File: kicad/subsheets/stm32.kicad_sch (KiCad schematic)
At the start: 11 parts, among them U3 STM32U575RGT6

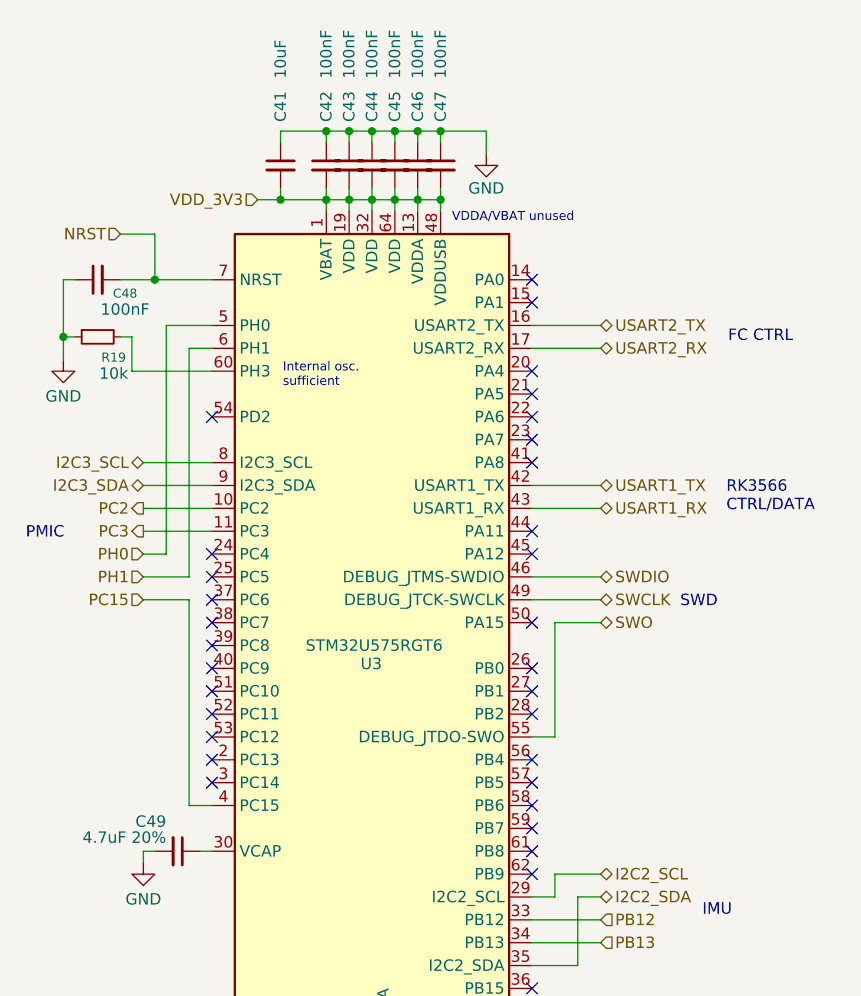
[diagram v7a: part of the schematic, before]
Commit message: Added boot + power switch to STM32, user button
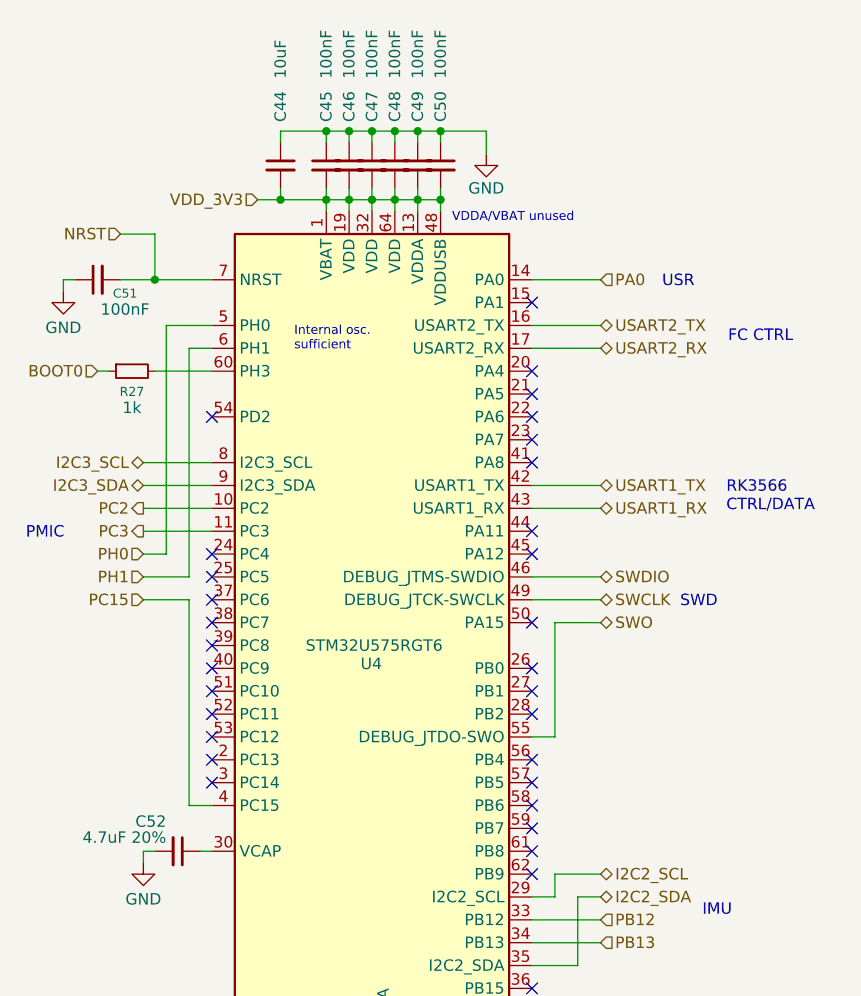
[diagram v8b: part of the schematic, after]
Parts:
- R27: renamed from R19; value 10k -> 1k
- renumbered C41 to C44, C42 to C45, C43 to C46, C44 to C47, C45 to C48, C46 to C49, C47 to C50, C48 to C51, C49 to C52, U3 to U4
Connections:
- net GND: no longer R27.1
- net PA0: now reaches U4.14 (PA0)
- new net BOOT0: R27.1
- no-connect marks 32 -> 31
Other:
- note added: "USR"
- moved on the sheet: R27
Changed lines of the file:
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@@
 		)
 	)
+	(text "USR"
+		(exclude_from_sim no)
+		(at 103.886 45.974 0)
+		(effects
+			(font
+				(size 1.27 1.27)
+			)
+		)
+	)
 	(text "RK3566 \nCTRL/DATA"
 		(exclude_from_sim no)
@@
 	(text "Internal osc.\nsufficient"
 		(exclude_from_sim no)
-		(at 59.944 56.388 0)
+		(at 61.214 52.324 0)
 		(effects
 			(font
@@
 	)
 	(junction
-		(at 35.56 52.07)
-		(diameter 0)
-		(color 0 0 0 0)
-	)
-	(junction
 		(at 45.72 45.72)
 		(diameter 0)
@@
 	)
 	(no_connect
-		(at 87.63 45.72)
-	)
-	(no_connect
 		(at 52.07 88.9)
 	)
@@
 	(wire
 		(pts
-			(xy 43.18 55.88) (xy 52.07 55.88)
-		)
-		(stroke
-			(width 0)
-			(type default)
-		)
-	)
-	(wire
-		(pts
 			(xy 44.45 76.2) (xy 46.99 76.2)
 		)
@@
 	(wire
 		(pts
-			(xy 35.56 54.61) (xy 35.56 52.07)
+			(xy 35.56 45.72) (xy 35.56 46.99)
 		)
 		(stroke
@@
 	(wire
 		(pts
-			(xy 41.91 52.07) (xy 43.18 52.07)
-		)
-		(stroke
-			(width 0)
-			(type default)
-		)
-	)
-	(wire
-		(pts
 			(xy 64.77 36.83) (xy 67.31 36.83)
 		)
@@
 	(wire
 		(pts
+			(xy 45.72 55.88) (xy 52.07 55.88)
+		)
+		(stroke
+			(width 0)
+			(type default)
+		)
+	)
+	(wire
+		(pts
 			(xy 74.93 35.56) (xy 74.93 36.83)
 		)
@@
 	(wire
 		(pts
-			(xy 35.56 52.07) (xy 36.83 52.07)
+			(xy 39.37 55.88) (xy 40.64 55.88)
 		)
 		(stroke
@@
 	(wire
 		(pts
-			(xy 43.18 52.07) (xy 43.18 55.88)
-		)
-		(stroke
-			(width 0)
-			(type default)
-		)
-	)
-	(wire
-		(pts
 			(xy 44.45 109.22) (xy 45.72 109.22)
 		)
@@
 	(wire
 		(pts
-			(xy 35.56 45.72) (xy 35.56 52.07)
+			(xy 44.45 68.58) (xy 52.07 68.58)
 		)
 		(stroke
@@
 	(wire
 		(pts
-			(xy 44.45 68.58) (xy 52.07 68.58)
+			(xy 68.58 132.08) (xy 68.58 133.35)
 		)
 		(stroke
@@
 	(wire
 		(pts
-			(xy 68.58 132.08) (xy 68.58 133.35)
+			(xy 95.25 45.72) (xy 87.63 45.72)
 		)
 		(stroke
@@
 		)
 	)
+	(hierarchical_label "BOOT0"
+		(shape input)
+		(at 39.37 55.88 180)
+		(effects
+			(font
+				(size 1.27 1.27)
+			)
+			(justify right)
+		)
+	)
 	(hierarchical_label "PC3"
 		(shape output)
@@
 		)
 	)
+	(hierarchical_label "PA0"
+		(shape input)
+		(at 95.25 45.72 0)
+		(effects
+			(font
+				(size 1.27 1.27)
+			)
+			(justify left)
+		)
+	)
 	(hierarchical_label "USART2_TX"
 		(shape bidirectional)
@@
 		(on_board yes)
 		(dnp no)
-		(property "Reference" "#PWR020"
+		(property "Reference" "#PWR031"
 			(at 44.45 116.84 0)
 			(effects
@@
 			(project "srad-camera"
 				(path "/da62c771-e8c9-451f-8df1-ec995aadcb11/cf8a0c2d-fb2b-4eaa-949d-0ddbf6dd7299"
-					(reference "#PWR020")
+					(reference "#PWR031")
 					(unit 1)
 				)
@@
 		(on_board yes)
 		(dnp no)
-		(property "Reference" "C45"
+		(property "Reference" "C48"
 			(at 72.39 28.194 90)
 			(effects
@@
 			(project "srad-camera"
 				(path "/da62c771-e8c9-451f-8df1-ec995aadcb11/cf8a0c2d-fb2b-4eaa-949d-0ddbf6dd7299"
-					(reference "C45")
+					(reference "C48")
 					(unit 1)
 				)
@@
 		(on_board yes)
 		(dnp no)
-		(property "Reference" "C44"
+		(property "Reference" "C47"
 			(at 69.85 28.194 90)
 			(effects
@@
 			(project "srad-camera"
 				(path "/da62c771-e8c9-451f-8df1-ec995aadcb11/cf8a0c2d-fb2b-4eaa-949d-0ddbf6dd7299"
-					(reference "C44")
+					(reference "C47")
 					(unit 1)
 				)
@@
 		(on_board yes)
 		(dnp no)
-		(property "Reference" "C48"
+		(property "Reference" "C51"
 			(at 42.418 47.244 90)
 			(effects
@@
 			(project "srad-camera"
 				(path "/da62c771-e8c9-451f-8df1-ec995aadcb11/cf8a0c2d-fb2b-4eaa-949d-0ddbf6dd7299"
-					(reference "C48")
+					(reference "C51")
 					(unit 1)
 				)
@@
 		(on_board yes)
 		(dnp no)
-		(property "Reference" "C42"
+		(property "Reference" "C45"
 			(at 64.77 28.194 90)
 			(effects
@@
 			(project "srad-camera"
 				(path "/da62c771-e8c9-451f-8df1-ec995aadcb11/cf8a0c2d-fb2b-4eaa-949d-0ddbf6dd7299"
-					(reference "C42")
+					(reference "C45")
 					(unit 1)
 				)
@@
 	(symbol
 		(lib_id "power:GND")
-		(at 35.56 54.61 0)
+		(at 35.56 46.99 0)
 		(unit 1)
 		(exclude_from_sim no)
@@
 		(on_board yes)
 		(dnp no)
-		(property "Reference" "#PWR019"
-			(at 35.56 60.96 0)
+		(property "Reference" "#PWR030"
+			(at 35.56 53.34 0)
 			(effects
 				(font
@@
 		)
 		(property "Value" "GND"
-			(at 35.56 58.674 0)
+			(at 35.56 51.054 0)
 			(effects
 				(font
@@
 		)
 		(property "Footprint" ""
-			(at 35.56 54.61 0)
+			(at 35.56 46.99 0)
 			(effects
 				(font
@@
 		)
 		(property "Datasheet" ""
-			(at 35.56 54.61 0)
+			(at 35.56 46.99 0)
 			(effects
 				(font
@@
 		)
 		(property "Description" "Power symbol creates a global label with name \"GND\" , ground"
-			(at 35.56 54.61 0)
+			(at 35.56 46.99 0)
 			(effects
 				(font
@@
 			(project "srad-camera"
 				(path "/da62c771-e8c9-451f-8df1-ec995aadcb11/cf8a0c2d-fb2b-4eaa-949d-0ddbf6dd7299"
-					(reference "#PWR019")
+					(reference "#PWR030")
 					(unit 1)
 				)
@@
 		(on_board yes)
 		(dnp no)
-		(property "Reference" "C47"
+		(property "Reference" "C50"
 			(at 77.47 28.194 90)
 			(effects
@@
 			(project "srad-camera"
 				(path "/da62c771-e8c9-451f-8df1-ec995aadcb11/cf8a0c2d-fb2b-4eaa-949d-0ddbf6dd7299"
-					(reference "C47")
+					(reference "C50")
 					(unit 1)
 				)
@@
 		(on_board yes)
 		(dnp no)
-		(property "Reference" "U3"
+		(property "Reference" "U4"
 			(at 68.58 88.392 0)
 			(effects
@@
 			(project "srad-camera"
 				(path "/da62c771-e8c9-451f-8df1-ec995aadcb11/cf8a0c2d-fb2b-4eaa-949d-0ddbf6dd7299"
-					(reference "U3")
+					(reference "U4")
 					(unit 1)
 				)
@@
 		(on_board yes)
 		(dnp no)
-		(property "Reference" "C43"
+		(property "Reference" "C46"
 			(at 67.31 28.194 90)
 			(effects
@@
 			(project "srad-camera"
 				(path "/da62c771-e8c9-451f-8df1-ec995aadcb11/cf8a0c2d-fb2b-4eaa-949d-0ddbf6dd7299"
-					(reference "C43")
+					(reference "C46")
 					(unit 1)
 				)
@@
 		(on_board yes)
 		(dnp no)
-		(property "Reference" "C41"
+		(property "Reference" "C44"
 			(at 59.69 28.194 90)
 			(effects
@@
 			(project "srad-camera"
 				(path "/da62c771-e8c9-451f-8df1-ec995aadcb11/cf8a0c2d-fb2b-4eaa-949d-0ddbf6dd7299"
-					(reference "C41")
+					(reference "C44")
 					(unit 1)
 				)
@@
 		(on_board yes)
 		(dnp no)
-		(property "Reference" "C49"
+		(property "Reference" "C52"
 			(at 46.99 105.918 90)
 			(effects
@@
 			(project "srad-camera"
 				(path "/da62c771-e8c9-451f-8df1-ec995aadcb11/cf8a0c2d-fb2b-4eaa-949d-0ddbf6dd7299"
-					(reference "C49")
+					(reference "C52")
 					(unit 1)
 				)
@@
 		(dnp no)
 		(fields_autoplaced yes)
-		(property "Reference" "#PWR021"
+		(property "Reference" "#PWR032"
 			(at 68.58 140.97 0)
 			(effects
@@
 			(project "srad-camera"
 				(path "/da62c771-e8c9-451f-8df1-ec995aadcb11/cf8a0c2d-fb2b-4eaa-949d-0ddbf6dd7299"
-					(reference "#PWR021")
+					(reference "#PWR032")
 					(unit 1)
 				)
@@
 		(on_board yes)
 		(dnp no)
-		(property "Reference" "#PWR018"
+		(property "Reference" "#PWR029"
 			(at 82.55 38.1 0)
 			(effects
@@
 			(project ""
 				(path "/da62c771-e8c9-451f-8df1-ec995aadcb11/cf8a0c2d-fb2b-4eaa-949d-0ddbf6dd7299"
-					(reference "#PWR018")
+					(reference "#PWR029")
 					(unit 1)
 				)
@@
 	(symbol
 		(lib_id "Device:R_Small")
-		(at 39.37 52.07 90)
+		(at 43.18 55.88 90)
 		(mirror x)
 		(unit 1)
@@
 		(on_board yes)
 		(dnp no)
-		(property "Reference" "R19"
-			(at 41.148 54.356 90)
+		(property "Reference" "R27"
+			(at 43.18 58.166 90)
 			(effects
 				(font
@@
 			)
 		)
-		(property "Value" "10k"
-			(at 41.148 56.134 90)
+		(property "Value" "1k"
+			(at 43.18 59.944 90)
 			(effects
 				(font
@@
 		)
 		(property "Footprint" ""
-			(at 39.37 52.07 0)
+			(at 43.18 55.88 0)
 			(effects
 				(font
@@
 		)
 		(property "Datasheet" "~"
-			(at 39.37 52.07 0)
+			(at 43.18 55.88 0)
 			(effects
 				(font
@@
 		)
 		(property "Description" "Resistor, small symbol"
-			(at 39.37 52.07 0)
+			(at 43.18 55.88 0)
 			(effects
 				(font
@@
 			(project "srad-camera"
 				(path "/da62c771-e8c9-451f-8df1-ec995aadcb11/cf8a0c2d-fb2b-4eaa-949d-0ddbf6dd7299"
-					(reference "R19")
+					(reference "R27")
 					(unit 1)
 				)
@@
 		(on_board yes)
 		(dnp no)
-		(property "Reference" "C46"
+		(property "Reference" "C49"
 			(at 74.93 28.194 90)
 			(effects
@@
 			(project "srad-camera"
 				(path "/da62c771-e8c9-451f-8df1-ec995aadcb11/cf8a0c2d-fb2b-4eaa-949d-0ddbf6dd7299"
-					(reference "C46")
+					(reference "C49")
 					(unit 1)
 				)
